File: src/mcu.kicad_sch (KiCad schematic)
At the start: 44 parts, among them J5 Conn_02x05_Odd_Even, J6 Conn_01x05_Pin, J7 1156915, U8 REF3033, U9 STM32F407VGTx, Y1 8MHz

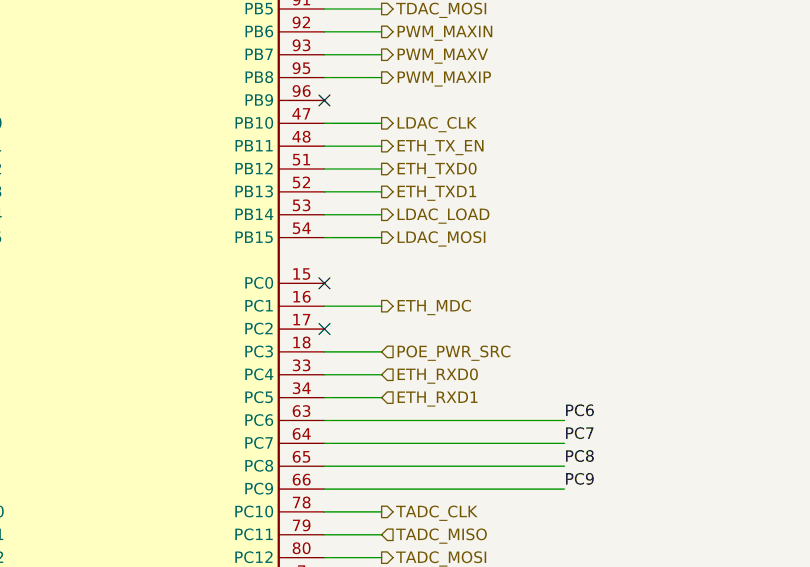
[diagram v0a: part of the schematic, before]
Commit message: sch, pcb: Add TDAC_VFB. Change 2u2 PMLCAP P/N - Connect TDAC voltage output through a RC LPF to MCU PC0(ADC123_IN10) - 2u2 PMLCAP P/N is changed to 16V version instead of 35V for lower cost
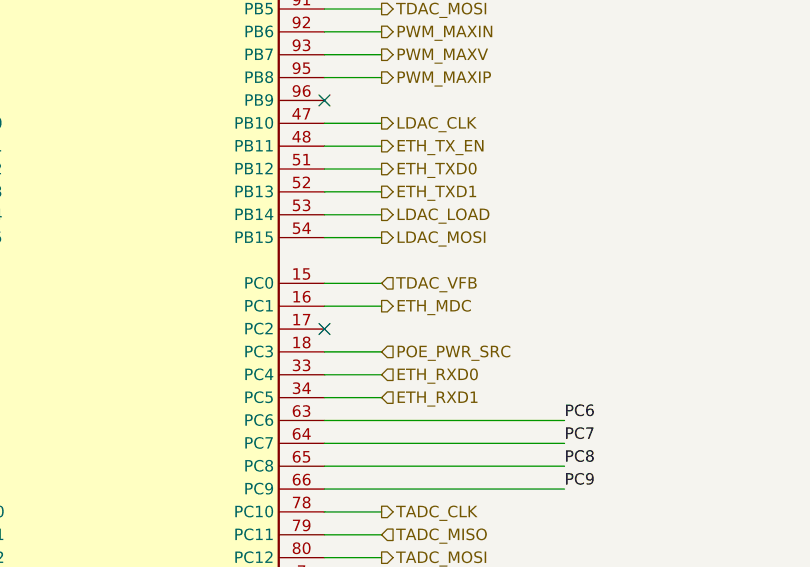
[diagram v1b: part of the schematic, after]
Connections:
- net TDAC_VFB: now reaches U9.15 (PC0)
- no-connect marks 25 -> 24
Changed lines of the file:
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@@
   (no_connect (at 226.06 172.72))
   (no_connect (at 226.06 101.6))
+  (no_connect (at 226.06 129.54))
   (no_connect (at 226.06 200.66))
   (no_connect (at 226.06 203.2))
   (no_connect (at 226.06 205.74))
   (no_connect (at 226.06 106.68))
-  (no_connect (at 226.06 129.54))
   (no_connect (at 180.34 129.54))
   (no_connect (at 180.34 124.46))
   (no_connect (at 180.34 127))
   (no_connect (at 226.06 147.32))
-  (no_connect (at 226.06 167.64))
   (no_connect (at 180.34 162.56))
   (no_connect (at 180.34 160.02))
@@
     (stroke (width 0) (type default))
   )
+  (wire (pts (xy 226.06 167.64) (xy 232.41 167.64))
+    (stroke (width 0) (type default))
+  )
   (wire (pts (xy 195.58 62.23) (xy 203.2 62.23))
     (stroke (width 0) (type default))
@@
     (effects (font (size 1.27 1.27)) (justify left))
   )
+  (hierarchical_label "TDAC_VFB" (shape input) (at 232.41 167.64 0) (fields_autoplaced)
+    (effects (font (size 1.27 1.27)) (justify left))
+  )

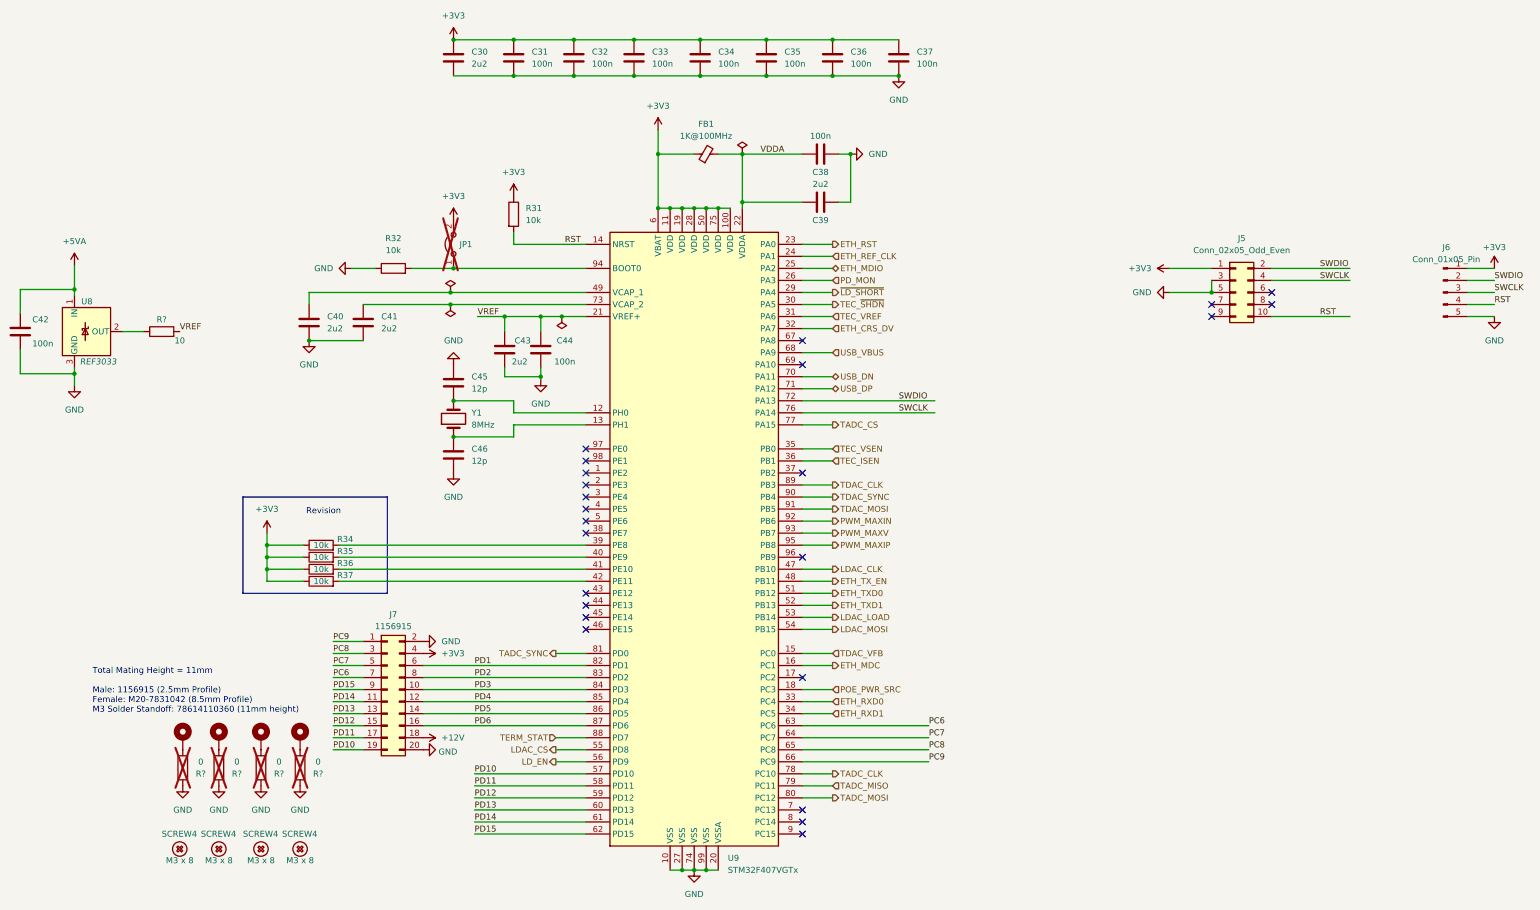
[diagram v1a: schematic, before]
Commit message: Fix issiues from lis, see bug/issiue list in DOC directory
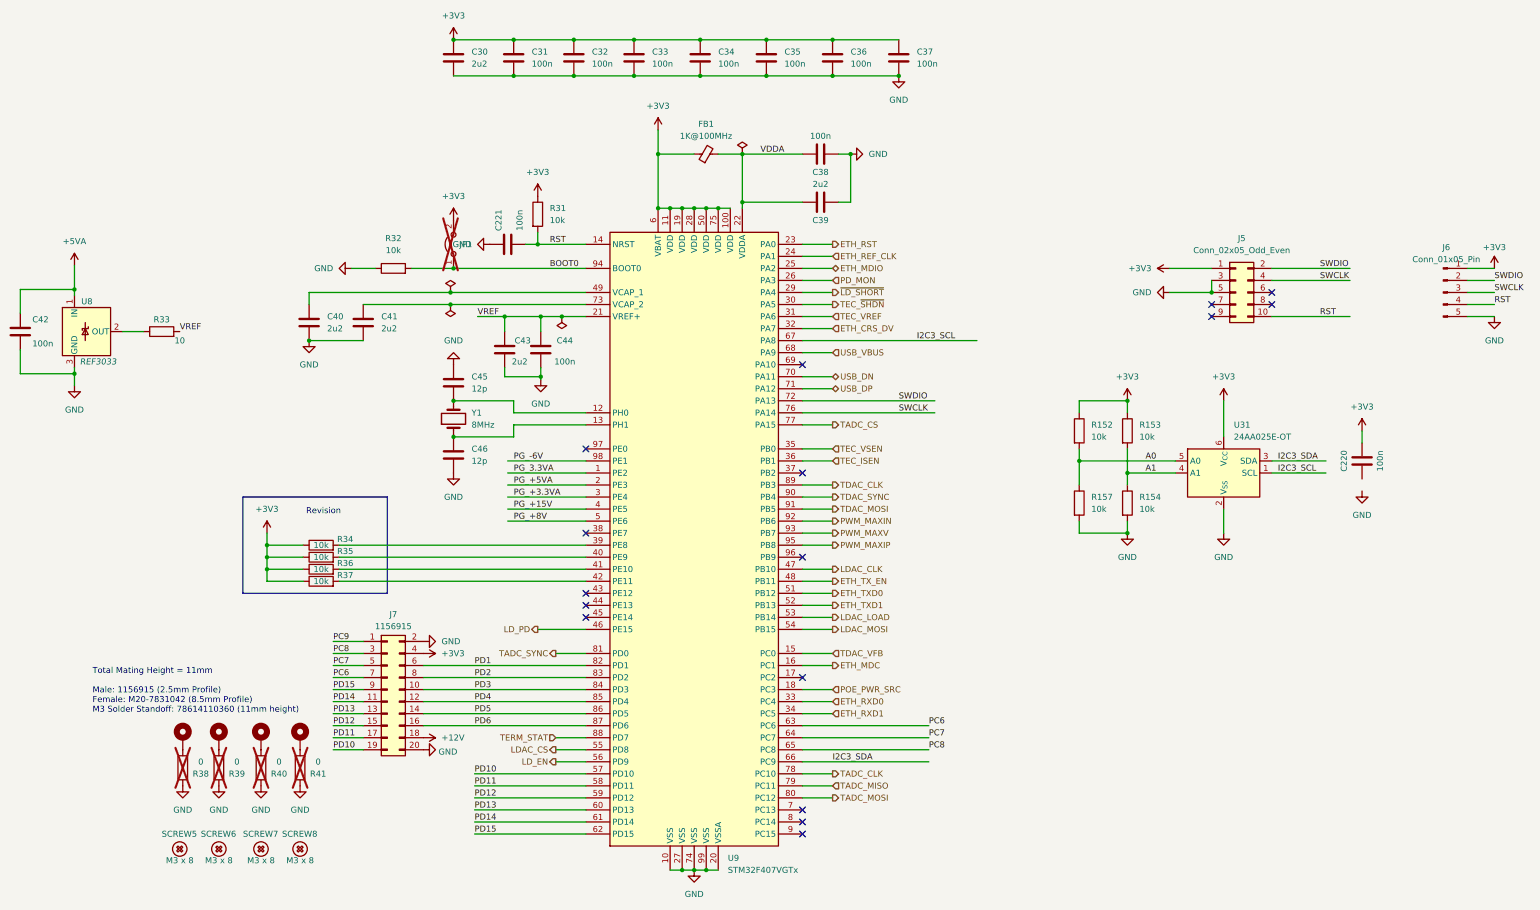
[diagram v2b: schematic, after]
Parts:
- added C220, C221: 100n, Capacitor_SMD:C_0603_1608Metric, symbol Device:C
- added R152, R153, R154, R157: 10k, Resistor_SMD:R_0603_1608Metric, symbol Device:R
- added U31: 24AA025E-OT, Package_TO_SOT_SMD:SOT-23-6, symbol Memory_EEPROM:24AA025E-OT
- gave numbers to parts that had none: 9
- renumbered SCREW4 to SCREW5, SCREW4 to SCREW6, SCREW4 to SCREW7, SCREW4 to SCREW8
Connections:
- net +3V3: now also C220.1, R152.1, R153.1, U31.6 (V_{CC})
- net GND: now also C221.2, R154.2, R157.2, U31.2 (V_{SS})
- net PC9: no longer U9.66 (PC9)
- net RST: now also C221.1
- net BOOT0: now reaches JP1.1 (A), R32.2, U9.94 (BOOT0)
- net PG_3.3VA: now reaches U9.1 (PE2)
- net PG_+5VA: now reaches U9.2 (PE3)
- net PG_+3.3VA: now reaches U9.3 (PE4)
- net PG_+15V: now reaches U9.4 (PE5)
- net LD_PD: now reaches U9.46 (PE15)
- net PG_+8V: now reaches U9.5 (PE6)
- net I2C3_SCL: now reaches U9.67 (PA8)
- net I2C3_SCL: now also U31.1 (SCL)
- net PG_-6V: now reaches U9.98 (PE1)
- new net A0: R152.2, R157.1, U31.5 (A0)
- new net A1: R153.2, R154.1, U31.4 (A1)
- new net I2C3_SDA: U31.3 (SDA), U9.66 (PC9)
- no-connect marks 24 -> 16
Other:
- moved on the sheet: R31
